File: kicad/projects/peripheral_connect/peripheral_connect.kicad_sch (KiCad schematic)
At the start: 17 parts, among them J1 peripheral_addr_bus_connector, J2 peripheral_aux_connector, J3 peripheral_membank_connector, J6 Conn_02x16_Odd_Even, J7 Conn_02x17_Odd_Even, J8 Conn_02x17_Odd_Even, U1 74HC138, U2 74HC138, U3 74HC238, U5 74HC238

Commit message: Rough layout of peripheral connect PCB.
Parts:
- added C5, C6, C7, C8: C, Capacitor_THT:C_Disc_D5.0mm_W2.5mm_P5.00mm, symbol Device:C
- added D1, D10, D11, D12, D13, D14, D15, D16, D17, D18, D19, D2, D20, D21, D22, D23, D24, D25, D26, D27, D28, D29, D3, D30, D31, D32, D4, D5, D6, D7, D8, D9: LED, sixteen-bit-computer:LED_D5.0mm_Horizontal_O3.81mm_Z3.0mm, symbol Device:LED
- added RN1, RN2, RN3, RN4: R_Network08_US, Resistor_THT:R_Array_SIP9, symbol Device:R_Network08_US
- added U4, U6, U7, U8: 74HC245, Package_DIP:DIP-20_W7.62mm_Socket, symbol sixteen-bit-computer:74HC245
- C1, C2, C3, C4: footprint (none) -> Capacitor_THT:C_Disc_D5.0mm_W2.5mm_P5.00mm
- J6: footprint (none) -> Connector_PinHeader_2.54mm:PinHeader_2x16_P2.54mm_Vertical
- J7: value Conn_02x17_Odd_Even -> ADDR; footprint (none) -> Connector_PinHeader_2.54mm:PinHeader_2x17_P2.54mm_Vertical
- J8: value Conn_02x17_Odd_Even -> DATA; footprint (none) -> Connector_PinHeader_2.54mm:PinHeader_2x17_P2.54mm_Vertical
- U1, U2, U3, U5: footprint (none) -> Package_DIP:DIP-16_W7.62mm_Socket
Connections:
- net ADDR_BUS_00: now also U3.1 (A0)
- net ADDR_BUS_01: now also U3.2 (A1)
- net ADDR_BUS_02: now also U3.3 (A2)
- net BANK_BUS_00: now also U4.9 (A8)
- net BANK_BUS_01: now also U4.8 (A7)
- net BANK_BUS_02: now also U4.7 (A6)
- net BANK_BUS_03: now also U4.6 (A5)
- net BANK_BUS_04: now also U4.5 (A3)
- net BANK_BUS_05: now also U4.4 (A3)
- net BANK_BUS_06: now also U4.3 (A2)
- net BANK_BUS_07: now also U4.2 (A1)
- net BANK_BUS_08: now also U6.9 (A8)
- net BANK_BUS_09: now also U6.8 (A7)
- net BANK_BUS_10: now also U6.7 (A6)
- net BANK_BUS_11: now also U6.6 (A5)
- net BANK_BUS_12: now also U6.5 (A3)
- net BANK_BUS_13: now also U6.4 (A3)
- net BANK_BUS_14: now also U6.3 (A2)
- net BANK_BUS_15: now also U6.2 (A1)
- net DEVICE_00: now also U7.9 (A8)
- net DEVICE_01: now also U7.8 (A7)
- net DEVICE_02: now also U7.7 (A6)
- net DEVICE_03: now also U7.6 (A5)
- net DEVICE_04: now also U7.5 (A3)
- net DEVICE_05: now also U7.4 (A3)
- net DEVICE_06: now also U7.3 (A2)
- net DEVICE_07: now also U7.2 (A1)
- net DEVICE_08: now also U8.9 (A8)
- net DEVICE_09: now also U8.8 (A7)
- net DEVICE_10: now also U8.7 (A6)
- net DEVICE_11: now also U8.6 (A5)
- net DEVICE_12: now also U8.5 (A3)
- net DEVICE_13: now also U8.4 (A3)
- net DEVICE_14: now also U8.3 (A2)
- net DEVICE_15: now also U8.2 (A1)
- net GND: now also C5.2, C6.1, C7.2, C8.1, U4.10 (GND), U6.10 (GND), U7.10 (GND), U8.10 (GND)
- net VCC: now also C5.1, C6.2, C7.1, C8.2, U4.1 (DIR), U4.20 (VCC), U6.1 (DIR), U6.20 (VCC), U7.1 (DIR), U7.20 (VCC), U8.1 (DIR), U8.20 (VCC)
- new net: D17.2 (A), U7.11 (B8)
- new net: D18.2 (A), U7.12 (B7)
- new net: D19.2 (A), U7.13 (B6)
- new net: D20.2 (A), U7.14 (B5)
- new net: D21.2 (A), U7.15 (B4)
- new net: D22.2 (A), U7.16 (B3)
- new net: D23.2 (A), U7.17 (B2)
- new net: D24.2 (A), U7.18 (B1)
- new net: D24.1 (K), RN3.2 (R1)
- new net: D23.1 (K), RN3.3 (R2)
- new net: D22.1 (K), RN3.4 (R3)
- new net: D21.1 (K), RN3.5 (R4)
- new net: D20.1 (K), RN3.6 (R5)
- new net: D19.1 (K), RN3.7 (R6)
- new net: D18.1 (K), RN3.8 (R7)
- new net: D17.1 (K), RN3.9 (R8)
- new net: D25.2 (A), U8.11 (B8)
- new net: D26.2 (A), U8.12 (B7)
- new net: D27.2 (A), U8.13 (B6)
- new net: D28.2 (A), U8.14 (B5)
- new net: D29.2 (A), U8.15 (B4)
- new net: D30.2 (A), U8.16 (B3)
- new net: D31.2 (A), U8.17 (B2)
- new net: D32.2 (A), U8.18 (B1)
- new net: D27.1 (K), RN4.7 (R6)
- new net: D28.1 (K), RN4.6 (R5)
- new net: D2.1 (K), RN1.8 (R7)
- new net: D2.2 (A), U4.12 (B7)
- new net: D32.1 (K), RN4.2 (R1)
- new net: D31.1 (K), RN4.3 (R2)
- new net: D30.1 (K), RN4.4 (R3)
- new net: D29.1 (K), RN4.5 (R4)
- new net: D26.1 (K), RN4.8 (R7)
- new net: D25.1 (K), RN4.9 (R8)
- new net: D6.1 (K), RN1.4 (R3)
- new net: D6.2 (A), U4.16 (B3)
- new net: D3.1 (K), RN1.7 (R6)
- new net: D3.2 (A), U4.13 (B6)
- new net: D5.1 (K), RN1.5 (R4)
- new net: D5.2 (A), U4.15 (B4)
- new net: D9.2 (A), U6.11 (B8)
- new net: D10.2 (A), U6.12 (B7)
- new net: D11.2 (A), U6.13 (B6)
- new net: D12.2 (A), U6.14 (B5)
- new net: D13.2 (A), U6.15 (B4)
- new net: D14.2 (A), U6.16 (B3)
- new net: D15.2 (A), U6.17 (B2)
- new net: D16.2 (A), U6.18 (B1)
- new net: D10.1 (K), RN2.8 (R7)
- new net: D14.1 (K), RN2.4 (R3)
- new net: D16.1 (K), RN2.2 (R1)
- new net: D15.1 (K), RN2.3 (R2)
- new net: D13.1 (K), RN2.5 (R4)
- new net: D12.1 (K), RN2.6 (R5)
- new net: D11.1 (K), RN2.7 (R6)
- new net: D9.1 (K), RN2.9 (R8)
- new net: D8.1 (K), RN1.2 (R1)
- new net: D8.2 (A), U4.18 (B1)
- new net: D1.1 (K), RN1.9 (R8)
- new net: D1.2 (A), U4.11 (B8)
- new net: D4.1 (K), RN1.6 (R5)
- new net: D4.2 (A), U4.14 (B5)
- new net: D7.1 (K), RN1.3 (R2)
- new net: D7.2 (A), U4.17 (B2)
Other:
- moved on the sheet: C1, C2, C3, C4, J6, J7, J8, U1, U2, U3, U5

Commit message: Un invert counter addressed. Almost done on peripheral connect PCB.
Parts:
- added J4: Conn_01x03_Pin, Connector_PinHeader_2.54mm:PinHeader_1x03_P2.54mm_Horizontal, symbol Connector:Conn_01x03_Pin
- added R1: 10K, Resistor_THT:R_Axial_DIN0207_L6.3mm_D2.5mm_P10.16mm_Horizontal, symbol Device:R_US
- RN1, RN2: value R_Network08_US -> 10K
- RN3, RN4: value R_Network08_US -> 1K
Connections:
- net GND: now also RN3.1 (common), RN4.1 (common), J4.3 (Pin_3), R1.2
- net VCC: now also RN1.1 (common), RN2.1 (common), J4.1 (Pin_1)
- net ~{LED ENABLE}: now reaches U7.19 (~{OE})
- net ~{LED ENABLE}: now also U4.19 (~{OE}), U6.19 (~{OE}), U8.19 (~{OE}), J4.2 (Pin_2), R1.1
- net at D2.1 (K): now also U4.12 (B7); no longer RN1.8 (R7)
- net at D2.2 (A): now also RN1.8 (R7); no longer U4.12 (B7)
- net at D6.1 (K): now also U4.16 (B3); no longer RN1.4 (R3)
- net at D6.2 (A): now also RN1.4 (R3); no longer U4.16 (B3)
- net at D3.1 (K): now also U4.13 (B6); no longer RN1.7 (R6)
- net at D3.2 (A): now also RN1.7 (R6); no longer U4.13 (B6)
- net at D5.1 (K): now also U4.15 (B4); no longer RN1.5 (R4)
- net at D5.2 (A): now also RN1.5 (R4); no longer U4.15 (B4)
- net at U6.11 (B8): now also D9.1 (K); no longer D9.2 (A)
- net at U6.12 (B7): now also D10.1 (K); no longer D10.2 (A)
- net at U6.13 (B6): now also D11.1 (K); no longer D11.2 (A)
- net at U6.14 (B5): now also D12.1 (K); no longer D12.2 (A)
- net at U6.15 (B4): now also D13.1 (K); no longer D13.2 (A)
- net at U6.16 (B3): now also D14.1 (K); no longer D14.2 (A)
- net at U6.17 (B2): now also D15.1 (K); no longer D15.2 (A)
- net at U6.18 (B1): now also D16.1 (K); no longer D16.2 (A)
- net at RN2.8 (R7): now also D10.2 (A); no longer D10.1 (K)
- net at RN2.4 (R3): now also D14.2 (A); no longer D14.1 (K)
- net at RN2.2 (R1): now also D16.2 (A); no longer D16.1 (K)
- net at RN2.3 (R2): now also D15.2 (A); no longer D15.1 (K)
- net at RN2.5 (R4): now also D13.2 (A); no longer D13.1 (K)
- net at RN2.6 (R5): now also D12.2 (A); no longer D12.1 (K)
- net at RN2.7 (R6): now also D11.2 (A); no longer D11.1 (K)
- net at RN2.9 (R8): now also D9.2 (A); no longer D9.1 (K)
- net at D8.1 (K): now also U4.18 (B1); no longer RN1.2 (R1)
- net at D8.2 (A): now also RN1.2 (R1); no longer U4.18 (B1)
- net at D1.1 (K): now also U4.11 (B8); no longer RN1.9 (R8)
- net at D1.2 (A): now also RN1.9 (R8); no longer U4.11 (B8)
- net at D4.1 (K): now also U4.14 (B5); no longer RN1.6 (R5)
- net at D4.2 (A): now also RN1.6 (R5); no longer U4.14 (B5)
- net at RN1.3 (R2): now also D7.2 (A); no longer D7.1 (K)
- net at U4.17 (B2): now also D7.1 (K); no longer D7.2 (A)
- no-connect marks 4 -> 9
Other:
- note added: "Address and data connections"
- note added: "Bank decode and LED display"
- note added: "Device decode and LED display"
- note added: "LED enable"
- moved on the sheet: C1, C2, C3, C4, C5, C6, C7, C8, C97, C98, C99, D1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

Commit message: Tech chekcs on Peripheral connect
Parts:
- C97, C98, C99: value C_Polarized -> 33uF
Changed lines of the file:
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@@
 (kicad_sch (version 20230121) (generator eeschema)
   (paper "B")
-  (bus_alias "DATA_BUS" (members "DATA_BUS_00" "DATA_BUS_01" "DATA_BUS_02" "DATA_BUS_03" "DATA_BUS_04" "DATA_BUS_05" "DATA_BUS_06" "DATA_BUS_07" "DATA_BUS_08" "DATA_BUS_09" "DATA_BUS_10" "DATA_BUS_11" "DATA_BUS_12" "DATA_BUS_13" "DATA_BUS_14" "DATA_BUS_15"))
   (bus_alias "BANK_BUS" (members "BANK_BUS_00" "BANK_BUS_01" "BANK_BUS_02" "BANK_BUS_03" "BANK_BUS_04" "BANK_BUS_05" "BANK_BUS_06" "BANK_BUS_07" "BANK_BUS_08" "BANK_BUS_09" "BANK_BUS_10" "BANK_BUS_11" "BANK_BUS_12" "BANK_BUS_13" "BANK_BUS_14" "BANK_BUS_15"))
+  (bus_alias "DATA_BUS" (members "DATA_BUS_00" "DATA_BUS_01" "DATA_BUS_02" "DATA_BUS_03" "DATA_BUS_04" "DATA_BUS_05" "DATA_BUS_06" "DATA_BUS_07" "DATA_BUS_08" "DATA_BUS_09" "DATA_BUS_10" "DATA_BUS_11" "DATA_BUS_12" "DATA_BUS_13" "DATA_BUS_14" "DATA_BUS_15"))
   (bus_alias "ADDR_BUS" (members "ADDR_BUS_00" "ADDR_BUS_01" "ADDR_BUS_02" "ADDR_BUS_03" "ADDR_BUS_04" "ADDR_BUS_05" "ADDR_BUS_06" "ADDR_BUS_07" "ADDR_BUS_08" "ADDR_BUS_09" "ADDR_BUS_10" "ADDR_BUS_11" "ADDR_BUS_12" "ADDR_BUS_13" "ADDR_BUS_14" "ADDR_BUS_15"))
   (junction (at 106.045 193.675) (diameter 0) (color 0 0 0 0)
@@
       (effects (font (size 1.27 1.27)) (justify left))
     )
-    (property "Value" "C_Polarized" (at 320.675 94.361 0)
+    (property "Value" "33uF" (at 320.675 94.361 0)
       (effects (font (size 1.27 1.27)) (justify left))
     )
@@
       (effects (font (size 1.27 1.27)) (justify left))
     )
-    (property "Value" "C_Polarized" (at 359.41 94.361 0)
+    (property "Value" "33uF" (at 359.41 94.361 0)
       (effects (font (size 1.27 1.27)) (justify left))
     )
@@
       (effects (font (size 1.27 1.27)) (justify left))
     )
-    (property "Value" "C_Polarized" (at 340.36 94.361 0)
+    (property "Value" "33uF" (at 340.36 94.361 0)
       (effects (font (size 1.27 1.27)) (justify left))
     )

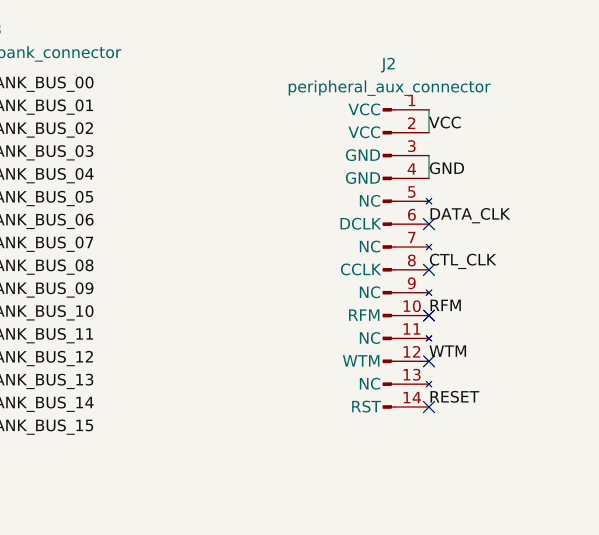
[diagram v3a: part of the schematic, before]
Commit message: Peripheral connect updated to one wire rfm wtm.
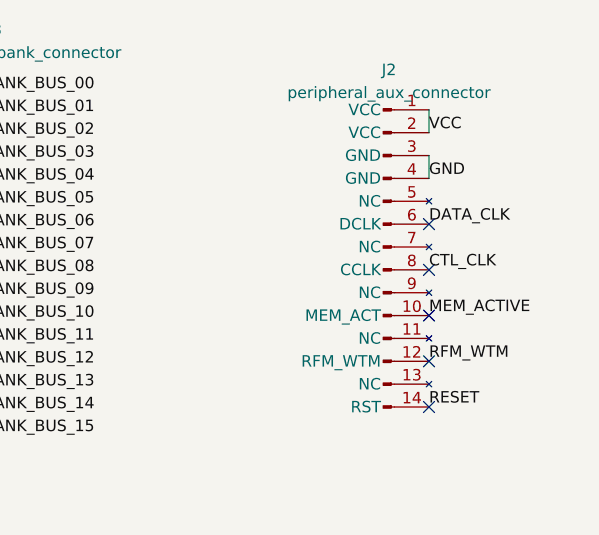
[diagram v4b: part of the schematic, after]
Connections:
- net RFM renamed MEM_ACTIVE
- net WTM renamed RFM_WTM
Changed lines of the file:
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@@
 (kicad_sch (version 20230121) (generator eeschema)
   (paper "B")
-  (bus_alias "BANK_BUS" (members "BANK_BUS_00" "BANK_BUS_01" "BANK_BUS_02" "BANK_BUS_03" "BANK_BUS_04" "BANK_BUS_05" "BANK_BUS_06" "BANK_BUS_07" "BANK_BUS_08" "BANK_BUS_09" "BANK_BUS_10" "BANK_BUS_11" "BANK_BUS_12" "BANK_BUS_13" "BANK_BUS_14" "BANK_BUS_15"))
   (bus_alias "DATA_BUS" (members "DATA_BUS_00" "DATA_BUS_01" "DATA_BUS_02" "DATA_BUS_03" "DATA_BUS_04" "DATA_BUS_05" "DATA_BUS_06" "DATA_BUS_07" "DATA_BUS_08" "DATA_BUS_09" "DATA_BUS_10" "DATA_BUS_11" "DATA_BUS_12" "DATA_BUS_13" "DATA_BUS_14" "DATA_BUS_15"))
   (bus_alias "ADDR_BUS" (members "ADDR_BUS_00" "ADDR_BUS_01" "ADDR_BUS_02" "ADDR_BUS_03" "ADDR_BUS_04" "ADDR_BUS_05" "ADDR_BUS_06" "ADDR_BUS_07" "ADDR_BUS_08" "ADDR_BUS_09" "ADDR_BUS_10" "ADDR_BUS_11" "ADDR_BUS_12" "ADDR_BUS_13" "ADDR_BUS_14" "ADDR_BUS_15"))
+  (bus_alias "BANK_BUS" (members "BANK_BUS_00" "BANK_BUS_01" "BANK_BUS_02" "BANK_BUS_03" "BANK_BUS_04" "BANK_BUS_05" "BANK_BUS_06" "BANK_BUS_07" "BANK_BUS_08" "BANK_BUS_09" "BANK_BUS_10" "BANK_BUS_11" "BANK_BUS_12" "BANK_BUS_13" "BANK_BUS_14" "BANK_BUS_15"))
   (junction (at 106.045 193.675) (diameter 0) (color 0 0 0 0)
   )
@@
     (effects (font (size 1.27 1.27)) (justify left bottom))
   )
-  (label "WTM" (at 347.98 56.515 0) (fields_autoplaced)
+  (label "RFM_WTM" (at 347.98 56.515 0) (fields_autoplaced)
     (effects (font (size 1.27 1.27)) (justify left bottom))
   )
@@
     (effects (font (size 1.27 1.27)) (justify left bottom))
   )
-  (label "RFM" (at 347.98 51.435 0) (fields_autoplaced)
+  (label "MEM_ACTIVE" (at 347.98 51.435 0) (fields_autoplaced)
     (effects (font (size 1.27 1.27)) (justify left bottom))
   )
@@
     )
   )
-  (symbol (lib_id "sixteen-bit-computer:peripheral_aux_connector") (at 342.9 43.815 0) (unit 1)
-    (in_bom yes) (on_board yes) (dnp no)
-    (property "Reference" "J2" (at 343.535 23.495 0)
+  (symbol (lib_id "Connector:Conn_01x03_Pin") (at 300.355 151.765 0) (unit 1)
+    (in_bom yes) (on_board yes) (dnp no) (fields_autoplaced)
+    (property "Reference" "J4" (at 300.99 144.78 0)
       (effects (font (size 1.27 1.27)))
     )
-    (property "Value" "peripheral_aux_connector" (at 343.535 26.035 0)
+    (property "Value" "Conn_01x03_Pin" (at 300.99 147.32 0)
       (effects (font (size 1.27 1.27)))
     )
-    (property "Footprint" "sixteen-bit-computer:peripheral-backplane-aux" (at 342.9 43.815 0)
+    (property "Footprint" "Connector_PinHeader_2.54mm:PinHeader_1x03_P2.54mm_Horizontal" (at 300.355 151.765 0)
       (effects (font (size 1.27 1.27)) hide)
     )
-    (property "Datasheet" "~" (at 342.9 43.815 0)
+    (property "Datasheet" "~" (at 300.355 151.765 0)
       (effects (font (size 1.27 1.27)) hide)
     )
     (pin "1")
-    (pin "10")
-    (pin "11")
-    (pin "12")
-    (pin "13")
-    (pin "14")
     (pin "2")
     (pin "3")
-    (pin "4")
-    (pin "5")
-    (pin "6")
-    (pin "7")
-    (pin "8")
-    (pin "9")
     (instances
       (project "peripheral_connect"
         (path "/0c25b387-1696-4e3f-ab8e-df646088b074"
-          (reference "J2") (unit 1)
+          (reference "J4") (unit 1)
         )
       )
     )
   )
-  (symbol (lib_id "Connector:Conn_01x03_Pin") (at 300.355 151.765 0) (unit 1)
+  (symbol (lib_id "sixteen-bit-computer:peripheral_aux_connector") (at 342.9 43.815 0) (unit 1)
     (in_bom yes) (on_board yes) (dnp no) (fields_autoplaced)
-    (property "Reference" "J4" (at 300.99 144.78 0)
+    (property "Reference" "J2" (at 343.535 24.13 0)
       (effects (font (size 1.27 1.27)))
     )
-    (property "Value" "Conn_01x03_Pin" (at 300.99 147.32 0)
+    (property "Value" "peripheral_aux_connector" (at 343.535 26.67 0)
       (effects (font (size 1.27 1.27)))
     )
-    (property "Footprint" "Connector_PinHeader_2.54mm:PinHeader_1x03_P2.54mm_Horizontal" (at 300.355 151.765 0)
+    (property "Footprint" "sixteen-bit-computer:peripheral-backplane-aux" (at 342.9 43.815 0)
       (effects (font (size 1.27 1.27)) hide)
     )
-    (property "Datasheet" "~" (at 300.355 151.765 0)
+    (property "Datasheet" "~" (at 342.9 43.815 0)
       (effects (font (size 1.27 1.27)) hide)
     )
     (pin "1")
+    (pin "10")
+    (pin "11")
+    (pin "12")
+    (pin "13")
+    (pin "14")
     (pin "2")
     (pin "3")
+    (pin "4")
+    (pin "5")
+    (pin "6")
+    (pin "7")
+    (pin "8")
+    (pin "9")
     (instances
       (project "peripheral_connect"
         (path "/0c25b387-1696-4e3f-ab8e-df646088b074"
-          (reference "J4") (unit 1)
+          (reference "J2") (unit 1)
         )
       )

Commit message: Add double row pin socket to peripheral connect.
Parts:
- J6: footprint Connector_PinHeader_2.54mm:PinHeader_2x16_P2.54mm_Vertical -> Connector_PinSocket_2.54mm:PinSocket_2x16_P2.54mm_Horizontal
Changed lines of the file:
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@@
       (effects (font (size 1.27 1.27)))
     )
-    (property "Footprint" "Connector_PinHeader_2.54mm:PinHeader_2x16_P2.54mm_Vertical" (at 112.395 69.215 0)
+    (property "Footprint" "Connector_PinSocket_2.54mm:PinSocket_2x16_P2.54mm_Horizontal" (at 112.395 69.215 0)
       (effects (font (size 1.27 1.27)) hide)
     )
